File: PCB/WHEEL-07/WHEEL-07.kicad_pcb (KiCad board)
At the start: 2 copper layers, 47 parts, among them IC1 TS5A21366DCUR, IC3 MP2332HGTL-P, IC4 NL27WZ14DTT1G, J10 BUTTON, J11 Conn_02x03_Counter_Clockwise, J2 SPI, J3 USART, J4 I2C, J5 PADDLE1, J6 PADDLE2, J7 BUTTON, J8 BUTTON, J9 BUTTON, U1 STM32F405RGTx, U2 MCP2561-E-SN, U3 MCP2561-E-SN, Y1 16Mhz, Y2 32KHz

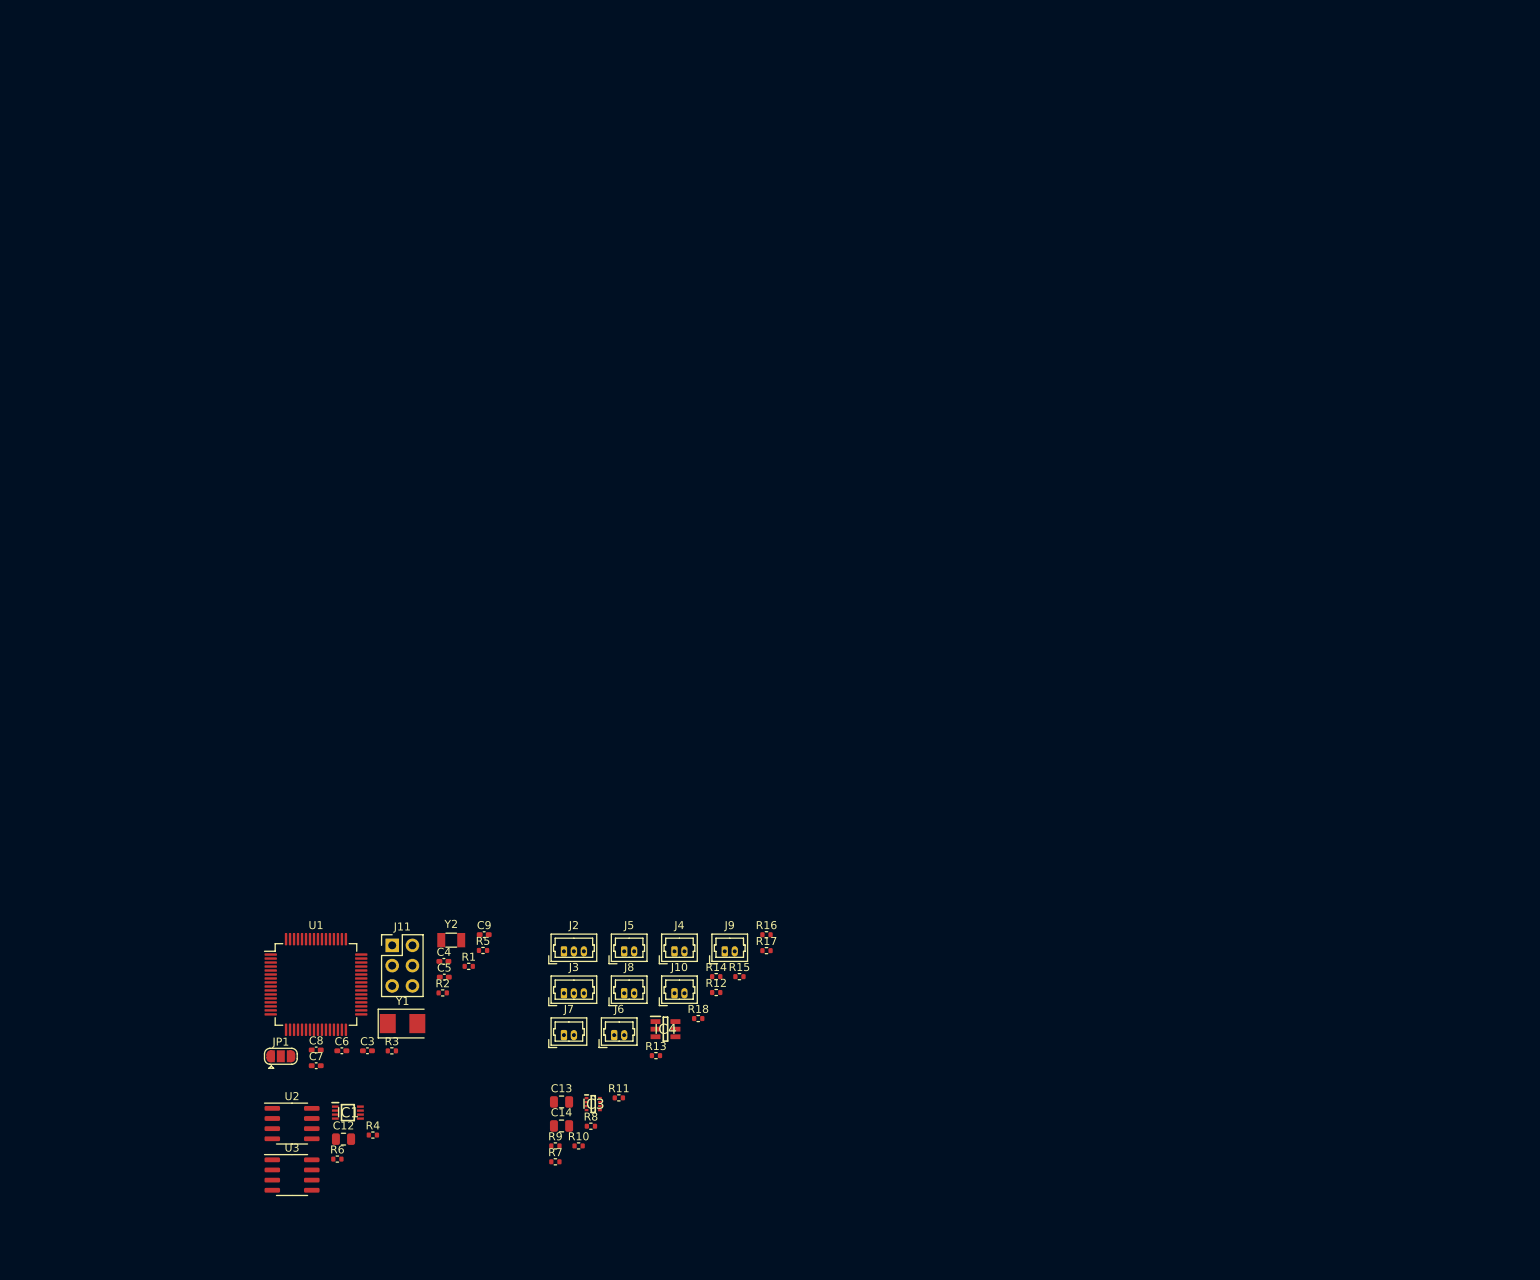
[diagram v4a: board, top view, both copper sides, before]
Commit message: Modified schematics & assigned all footprints
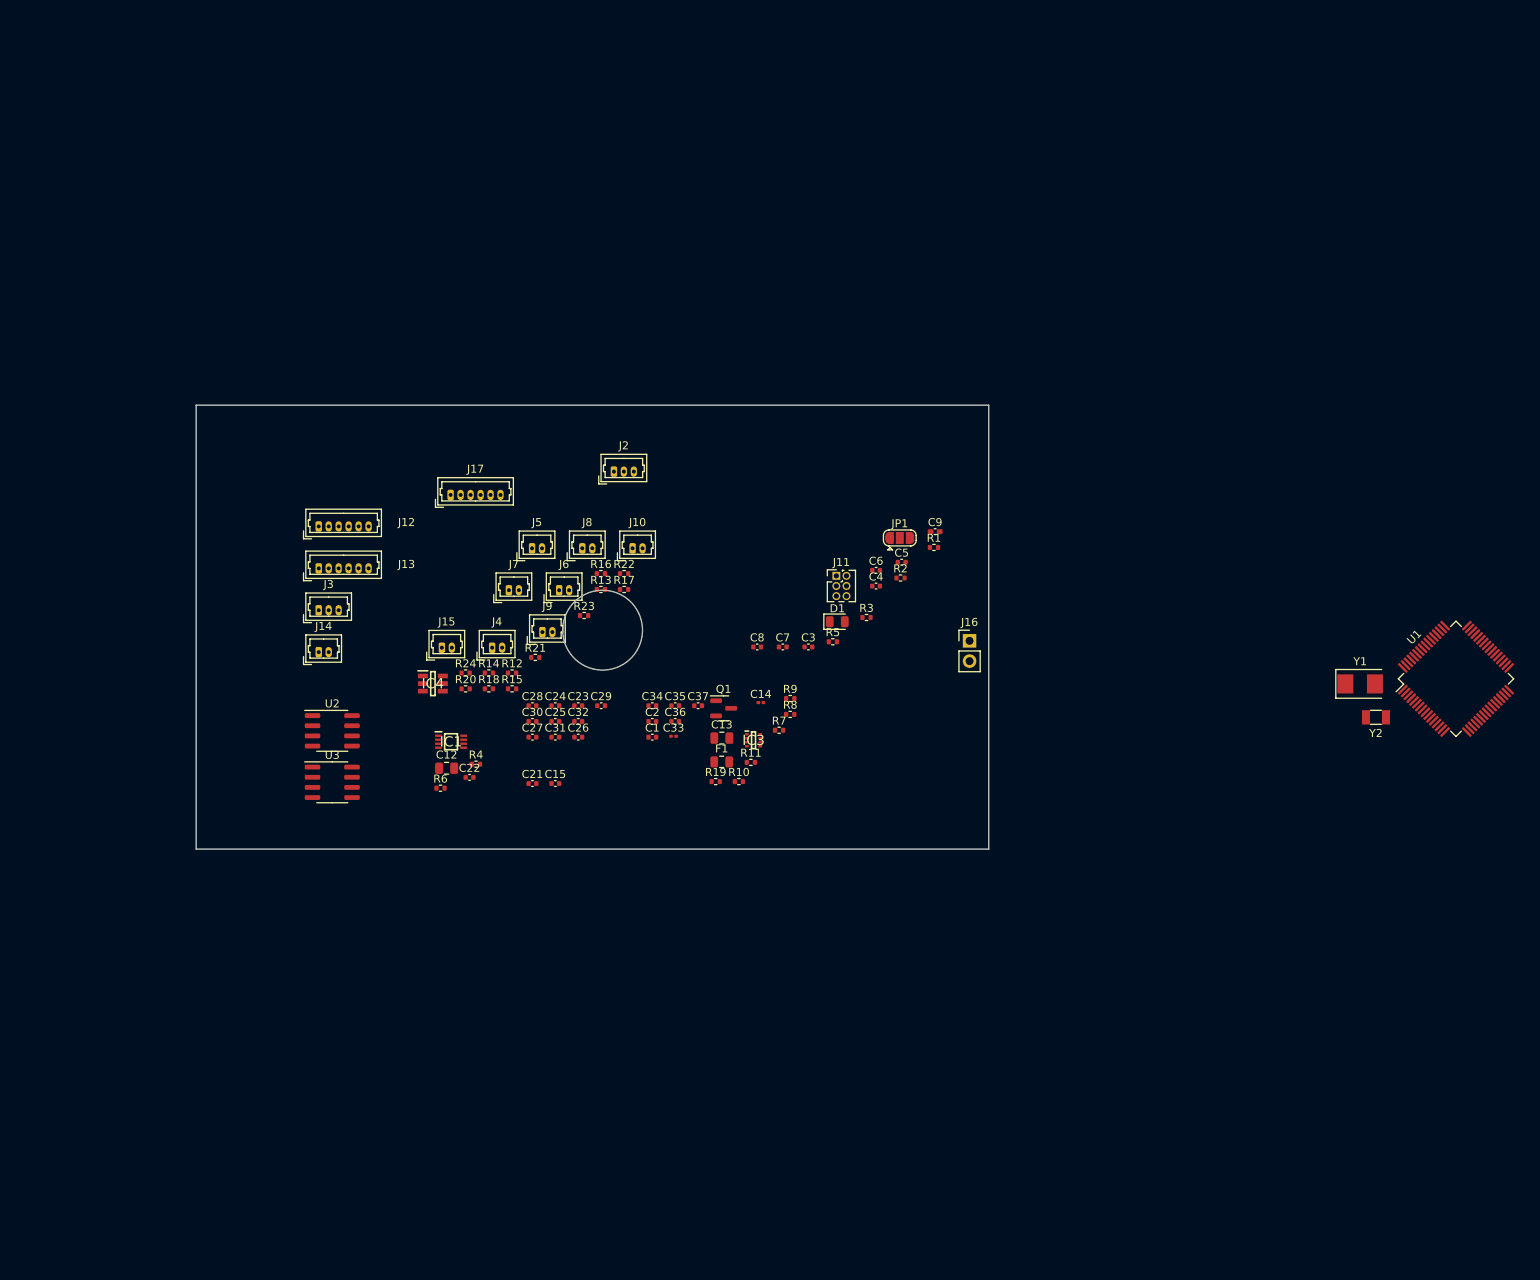
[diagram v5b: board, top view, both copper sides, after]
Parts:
- added C1: 2u2, Capacitor_SMD:C_0402_1005Metric, F.Cu at (129.7, 56.6)
- added C15: 22uF, Capacitor_SMD:C_0402_1005Metric, F.Cu at (117.5, 62.4)
- added C2: 2u2, Capacitor_SMD:C_0402_1005Metric, F.Cu at (129.7, 54.6)
- added C21: 22uF, Capacitor_SMD:C_0402_1005Metric, F.Cu at (114.7, 62.4)
- added C22: 22uF, Capacitor_SMD:C_0402_1005Metric, F.Cu at (106.8, 61.6)
- added C23: 100nF, Capacitor_SMD:C_0402_1005Metric, F.Cu at (120.4, 52.6)
- added C24: 100nF, Capacitor_SMD:C_0402_1005Metric, F.Cu at (117.5, 52.6)
- added C25: 10nF, Capacitor_SMD:C_0402_1005Metric, F.Cu at (117.5, 54.6)
- added C26: 10nF, Capacitor_SMD:C_0402_1005Metric, F.Cu at (120.4, 56.6)
- added C27: 10nF, Capacitor_SMD:C_0402_1005Metric, F.Cu at (114.7, 56.6)
- added C28: 10nF, Capacitor_SMD:C_0402_1005Metric, F.Cu at (114.7, 52.6)
- added C29: 10nF, Capacitor_SMD:C_0402_1005Metric, F.Cu at (123.3, 52.6)
- added C30: 10nF, Capacitor_SMD:C_0402_1005Metric, F.Cu at (114.7, 54.6)
- added C31: 10nF, Capacitor_SMD:C_0402_1005Metric, F.Cu at (117.5, 56.6)
- added C32: 10nF, Capacitor_SMD:C_0402_1005Metric, F.Cu at (120.4, 54.6)
- added C33: 4,7uF, Capacitor_SMD:C_0201_0603Metric, F.Cu at (132.3, 56.5)
- added C34: 100nF, Capacitor_SMD:C_0402_1005Metric, F.Cu at (129.7, 52.6)
- added C35: 100nF, Capacitor_SMD:C_0402_1005Metric, F.Cu at (132.5, 52.6)
- added C36: 100nF, Capacitor_SMD:C_0402_1005Metric, F.Cu at (132.5, 54.6)
- added C37: 100nF, Capacitor_SMD:C_0402_1005Metric, F.Cu at (135.4, 52.6)
- added D1: LED_Small, LED_SMD:LED_0805_2012Metric, F.Cu at (152.9, 42.1)
- added F1: Fuse, Fuse:Fuse_0805_2012Metric, F.Cu at (138.4, 59.7)
- added J12: ADC_B, Connector_Molex:Molex_PicoBlade_53047-0610_1x06_P1.25mm_Vertical, F.Cu at (87.9, 30.2)
- added J13: ADC_A, Connector_Molex:Molex_PicoBlade_53047-0610_1x06_P1.25mm_Vertical, F.Cu at (87.9, 35.4)
- added J14: BUTTON, Connector_Molex:Molex_PicoBlade_53047-0210_1x02_P1.25mm_Vertical, F.Cu at (87.9, 45.9)
- added J15: BUTTON, Connector_Molex:Molex_PicoBlade_53047-0210_1x02_P1.25mm_Vertical, F.Cu at (103.3, 45.4)
- added J16: POWER, Connector_PinHeader_2.54mm:PinHeader_1x02_P2.54mm_Vertical, F.Cu at (169.4, 44.5)
- added J17: TIM, Connector_Molex:Molex_PicoBlade_53047-0610_1x06_P1.25mm_Vertical, F.Cu at (104.4, 26.2)
- added Q1: AO3401A, Package_TO_SOT_SMD:SOT-23, F.Cu at (138.6, 53.0)
- added R19: 100, Resistor_SMD:R_0402_1005Metric, F.Cu at (137.6, 62.2)
- added R20: 1k, Resistor_SMD:R_0402_1005Metric, F.Cu at (106.3, 50.5)
- added R21: 1k, Resistor_SMD:R_0402_1005Metric, F.Cu at (115.0, 46.6)
- added R22: 1k, Resistor_SMD:R_0402_1005Metric, F.Cu at (126.1, 36.1)
- added R23: 1k, Resistor_SMD:R_0402_1005Metric, F.Cu at (121.1, 41.3)
- added R24: 1k, Resistor_SMD:R_0402_1005Metric, F.Cu at (106.3, 48.5)
- C12: value 0,1mF -> 0,1nF
- C14: footprint Capacitor_SMD:C_0805_2012Metric -> Capacitor_SMD:C_0201_0603Metric
- C3, C4, C5, C6, C7, C8: footprint Capacitor_SMD:C_0402_1005Metric_Pad0.74x0.62mm_HandSolder -> Capacitor_SMD:C_0402_1005Metric
- J11: value Conn_02x03_Counter_Clockwise -> DBG; footprint Connector_PinHeader_2.54mm:PinHeader_2x03_P2.54mm_Vertical -> Connector_PinHeader_1.27mm:PinHeader_2x03_P1.27mm_Vertical
- moved U1 147.9 mm to (230.4, 49.3), turned to 45 degrees
- moved Y1 127.3 mm to (218.4, 49.9)
- moved Y2 119.2 mm to (220.3, 54.1), turned to 180 degrees
- moved JP1 101.2 mm to (160.7, 31.6)
- moved C6 90.0 mm to (157.7, 35.7)
- moved R3 80.5 mm to (156.5, 41.6)
- moved C7 78.6 mm to (146.0, 45.3)
- moved R1 78.4 mm to (165.0, 32.8)
- moved R2 77.4 mm to (160.8, 36.6)
- moved C5 77.4 mm to (160.9, 34.7)
- moved C9 75.8 mm to (165.1, 30.8)
- moved C3 74.9 mm to (149.2, 45.3)
- moved C8 74.9 mm to (142.8, 45.3)
- moved J11 72.4 mm to (152.7, 36.4)
- moved C4 71.7 mm to (157.7, 37.7)
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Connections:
- U1 pad 37: TIM1_CH1 -> TIM3_CH1
- U1 pad 38: TIM1_CH2 -> TIM3_CH2
- U1 pad 39: TIM1_CH3 -> TIM3_CH3
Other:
- board outline added: 99.3 x 55.6 mm
- copper layers 2 -> 4

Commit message: Changed connectors setup
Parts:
- removed J13: ADC_A, Connector_Molex:Molex_PicoBlade_53047-0610_1x06_P1.25mm_Vertical
- removed J5: PADDLE1, Connector_Molex:Molex_PicoBlade_53047-0210_1x02_P1.25mm_Vertical
- removed J6: PADDLE2, Connector_Molex:Molex_PicoBlade_53047-0210_1x02_P1.25mm_Vertical
- added H1: MountingHole, MountingHole:MountingHole_2.2mm_M2, F.Cu at (157.1, 93.0)
- added H2: MountingHole, MountingHole:MountingHole_2.2mm_M2, F.Cu at (149.1, 53.3)
- added H4: MountingHole, MountingHole:MountingHole_2.2mm_M2, F.Cu at (197.9, 46.2)
- added IC2: LDO40LPU50RY, WHEEL-07:SON95P300X300X90-7N-D, F.Cu at (99.4, 53.0)
- added J**: 22057065, WHEEL-07:22057065, F.Cu at (152.1, 67.5)
- added L1: 2u7 120m, Inductor_SMD:L_0402_1005Metric, B.Cu at (177.4, 69.2)
- added REF**: Molex_PicoBlade_53048-0410_1x04_P1.25mm_Horizontal, Connector_Molex:Molex_PicoBlade_53048-0410_1x04_P1.25mm_Horizontal, F.Cu at (185.1, 81.0)
- C1, C15, C2, C21, C22, C23, C24, C3, C34, C35, C36, C37, C4, C5, C6: footprint Capacitor_SMD:C_0402_1005Metric -> Capacitor_SMD:C_0402_1005Metric_Pad0.74x0.62mm_HandSolder
- C12: footprint Capacitor_SMD:C_0805_2012Metric -> Capacitor_SMD:C_0402_1005Metric_Pad0.74x0.62mm_HandSolder
- C14: footprint Capacitor_SMD:C_0201_0603Metric -> Capacitor_SMD:C_0603_1608Metric
- C25, C26, C27, C28, C29, C30, C31, C32, C7, C8: footprint Capacitor_SMD:C_0402_1005Metric -> Capacitor_SMD:C_0402_1005Metric_Pad0.74x0.62mm_HandSolder; moved to B.Cu
- C33: footprint Capacitor_SMD:C_0201_0603Metric -> Capacitor_SMD:C_0603_1608Metric; moved to B.Cu
- C9, IC1, JP1: moved to B.Cu
- J12: value ADC_B -> Conn_01x10; footprint Connector_Molex:Molex_PicoBlade_53047-0610_1x06_P1.25mm_Vertical -> Connector_Molex:Molex_PicoBlade_53047-1010_1x10_P1.25mm_Vertical
- R1, R4, R6: footprint Resistor_SMD:R_0402_1005Metric -> Resistor_SMD:R_0402_1005Metric_Pad0.72x0.64mm_HandSolder; moved to B.Cu
- R10, R11, R12, R13, R14, R15, R16, R17, R18, R19, R2, R20, R21, R22, R23, R24, R3, R5, R7, R8, R9: footprint Resistor_SMD:R_0402_1005Metric -> Resistor_SMD:R_0402_1005Metric_Pad0.72x0.64mm_HandSolder
- Y1: footprint Crystal:Crystal_SMD_5032-2Pin_5.0x3.2mm -> Crystal:Crystal_SMD_2016-4Pin_2.0x1.6mm
- moved J14 111.0 mm to (194.3, 77.6), turned to 90 degrees
- moved C12 108.3 mm to (211.6, 48.8)
- moved J4 108.1 mm to (215.2, 68.4), turned to -90 degrees
- moved J12 106.7 mm to (180.8, 82.5), turned to 180 degrees
- moved J15 101.2 mm to (199.3, 77.6), turned to 90 degrees
- moved J2 100.2 mm to (217.1, 62.5)
- moved J7 98.5 mm to (199.4, 83.1), turned to 90 degrees
- moved J17 94.2 mm to (190.2, 65.1), turned to 90 degrees
- moved R13 91.7 mm to (214.0, 51.2)
- moved J8 87.5 mm to (199.2, 72.0), turned to 90 degrees
- moved IC4 86.6 mm to (184.5, 76.8), turned to 90 degrees
- moved R12 85.7 mm to (196.6, 62.6)
- moved J10 83.9 mm to (194.3, 83.3), turned to 90 degrees
- moved J9 83.4 mm to (194.3, 71.9), turned to 90 degrees
- moved U3 76.4 mm to (165.6, 54.4), turned to 180 degrees
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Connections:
- IC1 pad 2: /CAN_BUS/CAN1_H -> /CAN_BUS/CAN1_L
- IC1 pad 5: Net-(IC1-Pad5) -> /CAN_BUS/CAN2_H
- IC1 pad 6: /CAN_BUS/CAN2_H -> Net-(IC1-Pad6)
- J12 pad 1: GND -> +3.3V
- J12 pad 2: +3.3V -> GND
- R20 pad 1: ADC_A1 -> ADC_B1
- R21 pad 1: ADC_A2 -> ADC_B2
- R22 pad 1: ADC_A3 -> ADC_B3
- R23 pad 1: ADC_A4 -> ADC_B4
- R4 pad 1: /CAN_BUS/CAN1_L -> /CAN_BUS/CAN1_H
- R6 pad 2: Net-(IC1-Pad5) -> Net-(IC1-Pad6)
- U1 pad 56: CAN2_TERMINATOR_SW -> CAN1_TERMINATOR_SW
- U1 pad 59: CAN1_TERMINATOR_SW -> CAN2_TERMINATOR_SW
- Y1 pad 2: OSC_OUT -> GND
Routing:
- net GND: track 0.00 -> 38.1 mm, vias 0 -> 22
- net +3.3V: track 0.00 -> 18.9 mm, vias 0 -> 9
- net NRST: track 0.00 -> 17.0 mm, vias 0 -> 1
- net CAN2_RX: track 0.00 -> 13.0 mm
- net CAN1_TERMINATOR_SW: track 0.00 -> 11.6 mm, vias 0 -> 1
- net CAN2_TERMINATOR_SW: track 0.00 -> 10.7 mm, vias 0 -> 1
- net CAN2_TX: track 0.00 -> 9.43 mm
- net ADC_A1: track 0.00 -> 8.49 mm
- net OSC_OUT: track 0.00 -> 8.22 mm
- net OSC32_OUT: track 0.00 -> 8.18 mm
- net CAN1_RX: track 0.00 -> 7.99 mm
- net GPIO_7: track 0.00 -> 7.88 mm
- net ADC_A2: track 0.00 -> 7.82 mm
- net GPIO_8: track 0.00 -> 7.72 mm
- net GPIO_4: track 0.00 -> 7.53 mm
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- added copper zone on In2.Cu, net +3.3V
- added copper zone on In1.Cu, net GND
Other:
- board size 99.3 x 55.6 mm -> 54.7 x 34.8 mm

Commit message: Finished layout
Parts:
- removed C12: 0,1nF, Capacitor_SMD:C_0402_1005Metric_Pad0.74x0.62mm_HandSolder
- removed H1, H2, H4: MountingHole, MountingHole:MountingHole_2.2mm_M2
- removed IC1: TS5A21366DCUR, PDM_Additional:SOP50P310X90-8N
- removed J**: 22057065, WHEEL-07:22057065
- removed J3: USART, Connector_Molex:Molex_PicoBlade_53047-0310_1x03_P1.25mm_Vertical
- removed J4: I2C, Connector_Molex:Molex_PicoBlade_53047-0210_1x02_P1.25mm_Vertical
- removed R19: 100, Resistor_SMD:R_0402_1005Metric_Pad0.72x0.64mm_HandSolder
- removed REF**: Molex_PicoBlade_53048-0410_1x04_P1.25mm_Horizontal, Connector_Molex:Molex_PicoBlade_53048-0410_1x04_P1.25mm_Horizontal
- added C16: 1nF, Capacitor_SMD:C_0402_1005Metric_Pad0.74x0.62mm_HandSolder, F.Cu at (159.3, 78.9)
- added C17: 0.1uF, Capacitor_SMD:C_0402_1005Metric_Pad0.74x0.62mm_HandSolder, F.Cu at (159.3, 77.5)
- added C18: 6.8nF, Capacitor_SMD:C_0402_1005Metric_Pad0.74x0.62mm_HandSolder, F.Cu at (163.3, 79.9)
- added C19: 1uF, Capacitor_SMD:C_0402_1005Metric_Pad0.74x0.62mm_HandSolder, F.Cu at (163.3, 83.7)
- added C20: 10pF, Capacitor_SMD:C_0402_1005Metric_Pad0.74x0.62mm_HandSolder, F.Cu at (163.3, 74.8)
- added J1: Conn_01x06_Male, Connector_Molex:Molex_Micro-Latch_53254-0670_1x06_P2.00mm_Horizontal, F.Cu at (155.0, 71.7)
- added J5: Conn_01x04_Male, Connector_Molex:Molex_Micro-Latch_53254-0470_1x04_P2.00mm_Horizontal, F.Cu at (195.4, 78.9)
- added L2: 2.2uH, Inductor_SMD:L_Vishay_IHLP-1616, F.Cu at (154.6, 81.0)
- added kibuzzard-64076DC9: G***, kibuzzard-64076DC9, F.Cu at (184.5, 82.9)
- added kibuzzard-64076DD2: G***, kibuzzard-64076DD2, F.Cu at (198.9, 79.8)
- added kibuzzard-64076DF0: G***, kibuzzard-64076DF0, F.Cu at (150.5, 81.0)
- added kibuzzard-64076DFA: G***, kibuzzard-64076DFA, F.Cu at (154.2, 57.9)
- added kibuzzard-64076E40: G***, kibuzzard-64076E40, F.Cu at (176.3, 52.2)
- added kibuzzard-64076F6A: G***, kibuzzard-64076F6A, F.Cu at (192.5, 58.9)
- added kibuzzard-64135F75: G***, kibuzzard-64135F75, F.Cu at (170.7, 60.2)
- added kibuzzard-64135F81: G***, kibuzzard-64135F81, F.Cu at (170.7, 54.4)
- added kibuzzard-64137017: G***, kibuzzard-64137017, F.Cu at (193.3, 53.6)
- added kibuzzard-6414F4C6: G***, kibuzzard-6414F4C6, F.Cu at (185.0, 56.5)
- C15: footprint Capacitor_SMD:C_0402_1005Metric_Pad0.74x0.62mm_HandSolder -> Capacitor_SMD:C_0805_2012Metric
- C23, C24, R12, R13, R14, R15, R2, R3: moved to B.Cu
- J2: value SPI -> Conn_01x06_Male; footprint Connector_Molex:Molex_PicoBlade_53047-0310_1x03_P1.25mm_Vertical -> Connector_PinHeader_1.27mm:PinHeader_1x06_P1.27mm_Vertical
- R4, R6: moved to F.Cu
- moved C24 123.4 mm to (193.0, 81.5), turned to -90 degrees
- moved R15 120.3 mm to (194.3, 81.5), turned to -90 degrees
- moved C23 117.2 mm to (188.7, 81.5), turned to -90 degrees
- moved R14 115.5 mm to (190.0, 81.5), turned to -90 degrees
- moved R8 65.0 mm to (163.3, 82.4)
- moved R11 62.6 mm to (163.3, 76.1)
- moved F1 62.2 mm to (159.9, 73.4)
- moved Q1 61.9 mm to (159.8, 70.1), turned to 90 degrees
- moved R9 61.6 mm to (163.3, 78.6), turned to 180 degrees
- moved IC3 61.2 mm to (159.3, 81.1)
- moved R10 60.4 mm to (163.3, 77.4), turned to 180 degrees
- moved R7 60.2 mm to (163.3, 81.2)
- moved C15 58.8 mm to (159.9, 75.6), turned to 180 degrees
- moved IC2 55.0 mm to (154.3, 55.0)
- moved C14 53.2 mm to (158.1, 54.4), turned to 90 degrees
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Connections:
- J11 pad 3: +12V -> unconnected-(J11-Pad3)
- J17 pad 1: TIM3_CH3 -> TIM3_CH1
- J17 pad 3: TIM3_CH1 -> TIM3_CH3
- J2 pad 1: SPI_CS -> I2C2_SCL
- J2 pad 2: SPI2_SCK -> I2C2_SDA
- J2 pad 3: SPI2_MISO -> SPI_CS
- Q1 pad 1: Net-(Q1-Pad1) -> GND
- R12 pad 1: PADDLE1_IN -> PADDLE2_IN
- R13 pad 1: PADDLE2_IN -> PADDLE1_IN
- R14 pad 1: PADDLE1_IN -> PADDLE2_IN
- R15 pad 1: PADDLE2_IN -> PADDLE1_IN
- R4 pad 2: Net-(IC1-Pad1) -> /CAN_BUS/CAN1_L
- R6 pad 2: Net-(IC1-Pad6) -> /CAN_BUS/CAN2_H
- U1 pad 56: CAN1_TERMINATOR_SW -> unconnected-(U1-Pad56)
- U1 pad 59: CAN2_TERMINATOR_SW -> unconnected-(U1-Pad59)
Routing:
- net GND: track 38.1 -> 64.6 mm, vias 22 -> 45
- net TIM3_CH1: track 0.00 -> 14.4 mm
- net GPIO_3: track 6.57 -> 20.8 mm
- net TIM3_CH3: track 0.00 -> 14.2 mm
- net TIM3_CH2: track 0.00 -> 14.2 mm
- net Net-(C24-Pad1): track 0.00 -> 12.3 mm, vias 0 -> 1
- net I2C2_SCL: track 0.00 -> 12.0 mm, vias 0 -> 1
- net TIM1_CH3: track 0.00 -> 12.0 mm
- net TIM1_CH1: track 0.00 -> 12.0 mm
- net TIM1_CH2: track 0.00 -> 11.9 mm
- net GPIO_7: track 7.88 -> 19.5 mm
- net CAN1_TERMINATOR_SW: track 11.6 -> 0.00 mm, vias 1 -> 0
- net /CAN_BUS/CAN2_H: track 1.35 -> 12.5 mm, vias 1 -> 0
- net CAN2_TERMINATOR_SW: track 10.7 -> 0.00 mm, vias 1 -> 0
- net GPIO_5: track 7.44 -> 18.0 mm
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- added copper zone on F.Cu, net +12V
- added copper zone on F.Cu, net +3.3V
- added copper zone on F.Cu, net +5V
- added copper zone on In2.Cu, net +5V
- added copper zone on F.Cu, net GND
- added copper zone on F.Cu, net Net-(C19-Pad2)
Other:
- board size 54.7 x 34.8 mm -> 52.5 x 34.7 mm
- board text added: "3V3"
- board text added: "BOOT0"
- board text added: "CLK"
- board text added: "DIO"
- board text added: "GND"
- board text added: "by K.Pergol"
